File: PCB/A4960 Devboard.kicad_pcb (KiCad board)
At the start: 2 copper layers, 43.4 x 48.8 mm, 56 parts, among them IC1 ATMEGA8-AI, P1 CONN_02X03, P2 CONN_01X02, P3 CONN_01X03, P4 CONN_01X03, Q1 Q_NMOS_GDS_old, Q2 Q_NMOS_GDS_old, Q3 Q_NMOS_GDS_old, Q4 Q_NMOS_GDS_old, Q5 Q_NMOS_GDS_old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

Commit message: Mehr Vias!
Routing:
- net GND: track 121.4 -> 151.9 mm, vias 11 -> 35
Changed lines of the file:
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@@
     (thickness 1.6)
     (drawings 8)
-    (tracks 790)
+    (tracks 853)
     (zones 0)
     (modules 56)
@@
     (0 F.Cu signal)
     (31 B.Cu signal)
-    (32 B.Adhes user)
-    (33 F.Adhes user)
-    (34 B.Paste user)
-    (35 F.Paste user)
+    (32 B.Adhes user hide)
+    (33 F.Adhes user hide)
+    (34 B.Paste user hide)
+    (35 F.Paste user hide)
     (36 B.SilkS user)
     (37 F.SilkS user)
     (38 B.Mask user)
     (39 F.Mask user)
-    (40 Dwgs.User user)
-    (41 Cmts.User user)
-    (42 Eco1.User user)
-    (43 Eco2.User user)
+    (40 Dwgs.User user hide)
+    (41 Cmts.User user hide)
+    (42 Eco1.User user hide)
+    (43 Eco2.User user hide)
     (44 Edge.Cuts user)
     (45 Margin user)
-    (46 B.CrtYd user)
-    (47 F.CrtYd user)
-    (48 B.Fab user)
-    (49 F.Fab user)
+    (46 B.CrtYd user hide)
+    (47 F.CrtYd user hide)
+    (48 B.Fab user hide)
+    (49 F.Fab user hide)
   )
   (setup
@@
   (segment (start 210.439 102.489) (end 211.594 102.489) (width 0.254) (layer F.Cu) (net 1))
   (segment (start 209.328 103.6) (end 210.439 102.489) (width 0.254) (layer F.Cu) (net 1))
+  (segment (start 205.613 89.396) (end 207.76 89.396) (width 0.1524) (layer F.Cu) (net 2) (status 400000))
+  (segment (start 207.76 89.396) (end 207.772 89.408) (width 0.1524) (layer F.Cu) (net 2))
+  (via (at 207.772 89.408) (size 0.6) (drill 0.4) (layers F.Cu B.Cu) (net 2))
+  (segment (start 207.772 89.408) (end 208.788 89.408) (width 0.1524) (layer B.Cu) (net 2))
+  (via (at 208.788 89.408) (size 0.6) (drill 0.4) (layers F.Cu B.Cu) (net 2))
+  (segment (start 208.788 89.408) (end 209.804 89.408) (width 0.1524) (layer F.Cu) (net 2))
+  (via (at 209.804 89.408) (size 0.6) (drill 0.4) (layers F.Cu B.Cu) (net 2))
+  (segment (start 209.804 89.408) (end 210.82 89.408) (width 0.1524) (layer B.Cu) (net 2))
+  (via (at 210.82 89.408) (size 0.6) (drill 0.4) (layers F.Cu B.Cu) (net 2))
+  (segment (start 203.402 84.074) (end 203.402 82.348) (width 0.1524) (layer F.Cu) (net 2) (status 400000))
+  (segment (start 203.402 82.348) (end 203.454 82.296) (width 0.1524) (layer F.Cu) (net 2))
+  (via (at 203.454 82.296) (size 0.6) (drill 0.4) (layers F.Cu B.Cu) (net 2))
+  (segment (start 203.454 82.296) (end 204.47 82.296) (width 0.1524) (layer B.Cu) (net 2))
+  (via (at 204.47 82.296) (size 0.6) (drill 0.4) (layers F.Cu B.Cu) (net 2))
+  (segment (start 204.47 82.296) (end 205.486 82.296) (width 0.1524) (layer F.Cu) (net 2))
+  (via (at 205.486 82.296) (size 0.6) (drill 0.4) (layers F.Cu B.Cu) (net 2))
+  (segment (start 205.486 82.296) (end 204.978 81.788) (width 0.1524) (layer B.Cu) (net 2))
+  (segment (start 204.978 81.788) (end 204.978 81.407) (width 0.1524) (layer B.Cu) (net 2))
+  (via (at 204.978 81.407) (size 0.6) (drill 0.4) (layers F.Cu B.Cu) (net 2))
+  (segment (start 204.978 81.407) (end 203.962 81.407) (width 0.1524) (layer F.Cu) (net 2))
+  (via (at 203.962 81.407) (size 0.6) (drill 0.4) (layers F.Cu B.Cu) (net 2))
+  (segment (start 203.962 81.407) (end 202.946 81.407) (width 0.1524) (layer B.Cu) (net 2))
+  (via (at 202.946 81.407) (size 0.6) (drill 0.4) (layers F.Cu B.Cu) (net 2))
+  (segment (start 202.946 81.407) (end 202.438 81.915) (width 0.1524) (layer F.Cu) (net 2))
+  (segment (start 202.438 81.915) (end 202.438 82.296) (width 0.1524) (layer F.Cu) (net 2))
+  (via (at 202.438 82.296) (size 0.6) (drill 0.4) (layers F.Cu B.Cu) (net 2))
+  (segment (start 215.646 100.33) (end 215.519 100.33) (width 0.1524) (layer B.Cu) (net 2))
+  (segment (start 215.519 100.33) (end 215.392 100.203) (width 0.1524) (layer B.Cu) (net 2))
+  (via (at 215.392 100.203) (size 0.6) (drill 0.4) (layers F.Cu B.Cu) (net 2))
+  (segment (start 216.916 101.727) (end 216.154 100.965) (width 0.1524) (layer F.Cu) (net 2))
+  (via (at 216.154 100.965) (size 0.6) (drill 0.4) (layers F.Cu B.Cu) (net 2))
+  (segment (start 216.154 100.965) (end 215.519 100.33) (width 0.1524) (layer B.Cu) (net 2))
+  (segment (start 215.519 100.33) (end 215.519 100.203) (width 0.1524) (layer B.Cu) (net 2))
+  (segment (start 217.932 101.727) (end 216.916 101.727) (width 0.1524) (layer B.Cu) (net 2))
+  (via (at 216.916 101.727) (size 0.6) (drill 0.4) (layers F.Cu B.Cu) (net 2))
+  (segment (start 218.694 102.489) (end 217.932 101.727) (width 0.1524) (layer F.Cu) (net 2))
+  (via (at 217.932 101.727) (size 0.6) (drill 0.4) (layers F.Cu B.Cu) (net 2))
+  (segment (start 217.932 101.727) (end 218.186 101.981) (width 0.1524) (layer B.Cu) (net 2))
+  (segment (start 218.186 101.981) (end 218.186 102.108) (width 0.1524) (layer B.Cu) (net 2))
+  (segment (start 218.948 102.108) (end 218.948 102.743) (width 0.1524) (layer B.Cu) (net 2))
+  (segment (start 218.948 102.743) (end 219.456 103.251) (width 0.1524) (layer B.Cu) (net 2))
+  (via (at 219.456 103.251) (size 0.6) (drill 0.4) (layers F.Cu B.Cu) (net 2))
+  (segment (start 219.456 103.251) (end 218.694 102.489) (width 0.1524) (layer F.Cu) (net 2))
+  (via (at 218.694 102.489) (size 0.6) (drill 0.4) (layers F.Cu B.Cu) (net 2))
+  (segment (start 218.694 102.489) (end 218.948 102.235) (width 0.1524) (layer B.Cu) (net 2))
+  (segment (start 218.948 102.235) (end 218.948 102.108) (width 0.1524) (layer B.Cu) (net 2))
+  (segment (start 202.819 75.946) (end 203.835 75.946) (width 0.1524) (layer F.Cu) (net 2))
+  (via (at 203.835 75.946) (size 0.6) (drill 0.4) (layers F.Cu B.Cu) (net 2))
+  (segment (start 205.867 75.382) (end 205.796 75.382) (width 0.1524) (layer F.Cu) (net 2) (status C00000))
+  (segment (start 205.796 75.382) (end 204.343 76.835) (width 0.1524) (layer F.Cu) (net 2) (status 400000))
+  (via (at 204.343 76.835) (size 0.6) (drill 0.4) (layers F.Cu B.Cu) (net 2))
+  (segment (start 204.343 76.835) (end 203.327 76.835) (width 0.1524) (layer B.Cu) (net 2))
+  (via (at 203.327 76.835) (size 0.6) (drill 0.4) (layers F.Cu B.Cu) (net 2))
+  (segment (start 203.327 76.835) (end 202.311 76.835) (width 0.1524) (layer F.Cu) (net 2))
+  (via (at 202.311 76.835) (size 0.6) (drill 0.4) (layers F.Cu B.Cu) (net 2))
+  (segment (start 202.311 76.835) (end 201.295 76.835) (width 0.1524) (layer B.Cu) (net 2))
+  (via (at 201.295 76.835) (size 0.6) (drill 0.4) (layers F.Cu B.Cu) (net 2))
+  (segment (start 201.295 76.835) (end 201.803 76.327) (width 0.1524) (layer F.Cu) (net 2))
+  (segment (start 201.803 76.327) (end 201.803 75.946) (width 0.1524) (layer F.Cu) (net 2))
+  (via (at 201.803 75.946) (size 0.6) (drill 0.4) (layers F.Cu B.Cu) (net 2))
+  (segment (start 201.803 75.946) (end 202.819 75.946) (width 0.1524) (layer B.Cu) (net 2))
+  (via (at 202.819 75.946) (size 0.6) (drill 0.4) (layers F.Cu B.Cu) (net 2))
+  (segment (start 202.819 75.946) (end 203.835 75.946) (width 0.1524) (layer F.Cu) (net 2))
   (segment (start 224.282 99.06) (end 225.171 99.06) (width 0.508) (layer B.Cu) (net 2))
   (segment (start 225.171 99.06) (end 224.536 98.425) (width 0.508) (layer F.Cu) (net 2))
@@
   (segment (start 200.781 97.35) (end 200.781 95.891) (width 0.1524) (layer F.Cu) (net 41))
   (segment (start 200.781 95.891) (end 200.648 95.758) (width 0.1524) (layer F.Cu) (net 41))
-  (segment (start 214.376 84.201) (end 214.376 85.344) (width 0.1524) (layer F.Cu) (net 42) (status 400000))
+  (segment (start 214.376 84.201) (end 214.376 85.344) (width 0.1524) (layer F.Cu) (net 42))
   (segment (start 214.376 85.344) (end 214.63 85.598) (width 0.1524) (layer F.Cu) (net 42))
   (via (at 214.63 85.598) (size 0.6) (drill 0.4) (layers F.Cu B.Cu) (net 42))
@@
   (segment (start 214.122 86.487) (end 215.138 86.487) (width 0.1524) (layer B.Cu) (net 42))
   (via (at 215.138 86.487) (size 0.6) (drill 0.4) (layers F.Cu B.Cu) (net 42))
-  (segment (start 227.838 84.074) (end 227.838 85.344) (width 0.1524) (layer F.Cu) (net 42) (status 400000))
+  (segment (start 227.838 84.074) (end 227.838 85.344) (width 0.1524) (layer F.Cu) (net 42))
   (segment (start 227.838 85.344) (end 227.965 85.471) (width 0.1524) (layer F.Cu) (net 42))
   (via (at 227.965 85.471) (size 0.6) (drill 0.4) (layers F.Cu B.Cu) (net 42))
@@
   (segment (start 229.489 86.36) (end 228.473 86.36) (width 0.1524) (layer B.Cu) (net 42))
   (via (at 228.473 86.36) (size 0.6) (drill 0.4) (layers F.Cu B.Cu) (net 42))
-  (segment (start 221.488 84.201) (end 221.488 85.725) (width 0.1524) (layer F.Cu) (net 42) (status 400000))
+  (segment (start 221.488 84.201) (end 221.488 85.725) (width 0.1524) (layer F.Cu) (net 42))
   (via (at 221.488 85.725) (size 0.6) (drill 0.4) (layers F.Cu B.Cu) (net 42))
   (segment (start 221.488 85.725) (end 222.504 85.725) (width 0.1524) (layer B.Cu) (net 42))

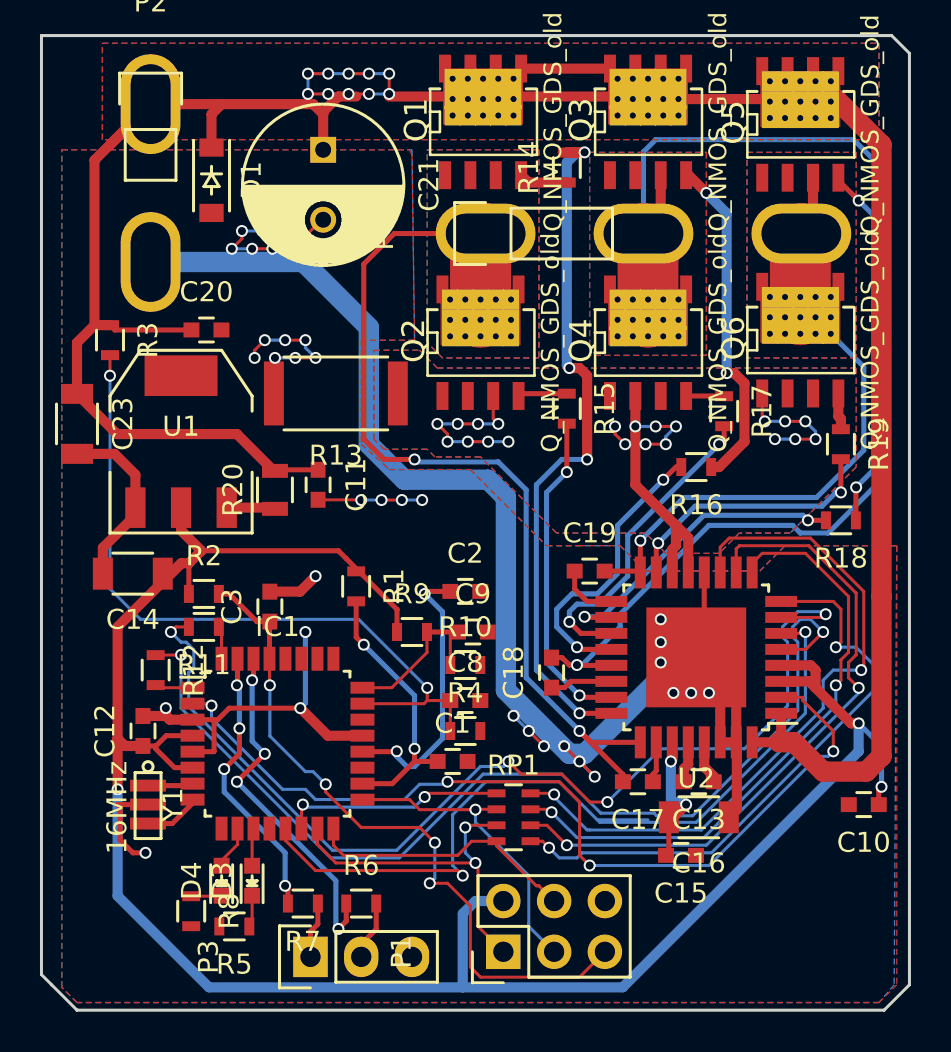
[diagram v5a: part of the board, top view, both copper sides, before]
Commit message: Bestückungsdruck und Befestigungsbohrungen
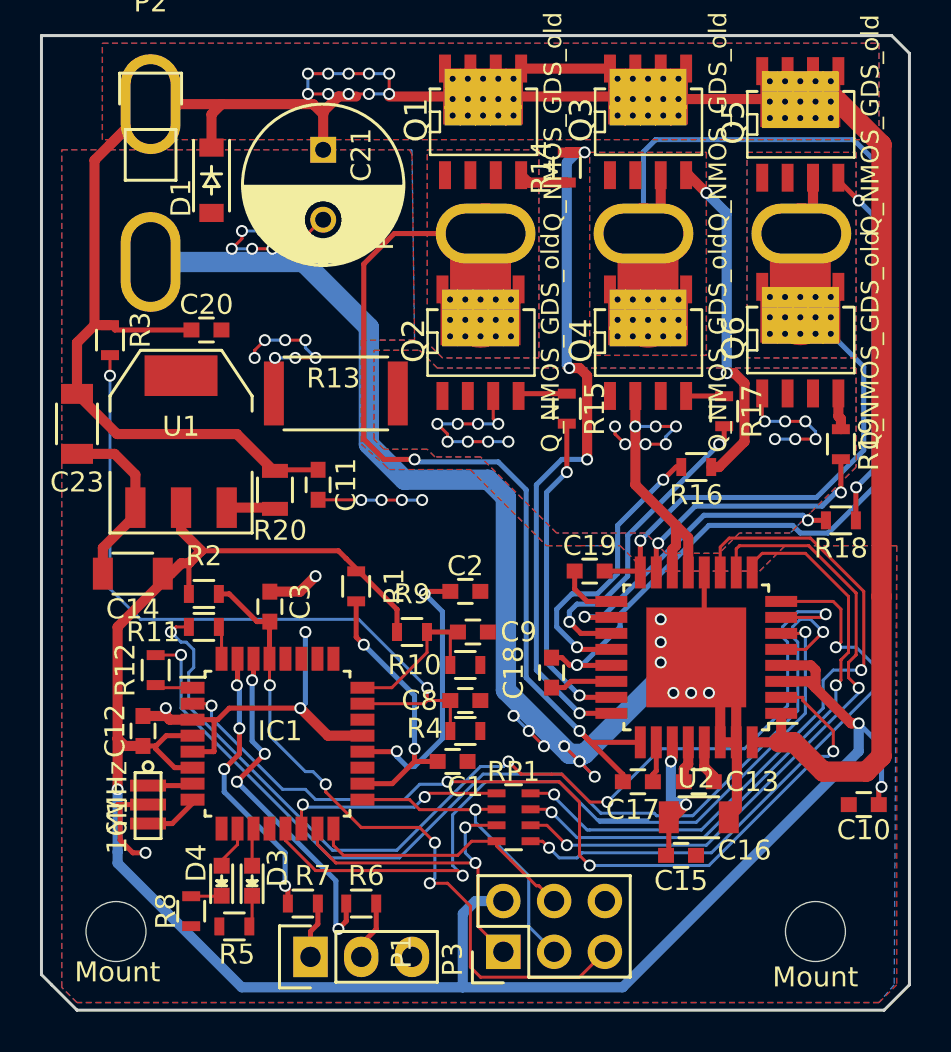
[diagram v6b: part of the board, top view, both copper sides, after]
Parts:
- added Mount: MountingHole_3mm, Mounting_Holes:MountingHole_3mm, F.Cu at (230.5, 111.0)
- added Mount: MountingHole_3mm, Mounting_Holes:MountingHole_3mm, F.Cu at (195.5, 111.0)
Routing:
- net +3V3: track 110.6 -> 109.7 mm
